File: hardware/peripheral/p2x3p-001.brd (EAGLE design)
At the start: 18 x 31 mm, 4 parts, among them J4 RLY

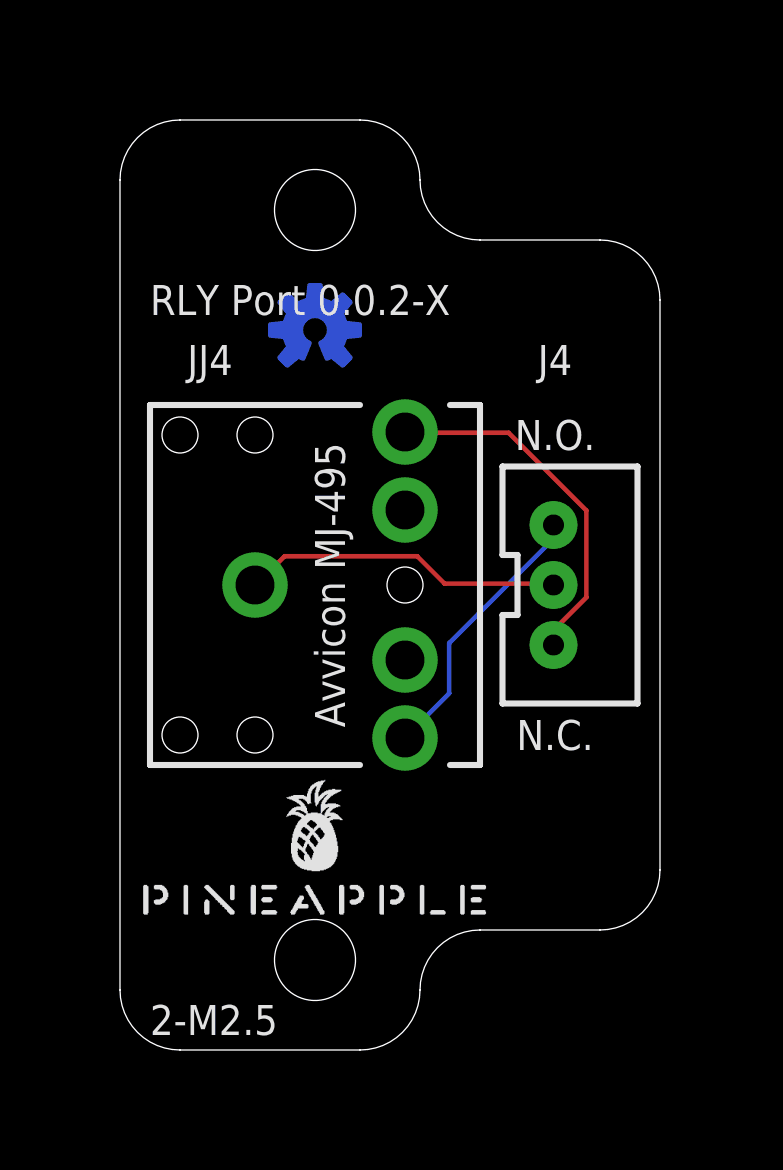
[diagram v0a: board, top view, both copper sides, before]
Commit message: Imported (again) from Hex Sw 0.0.2-X.
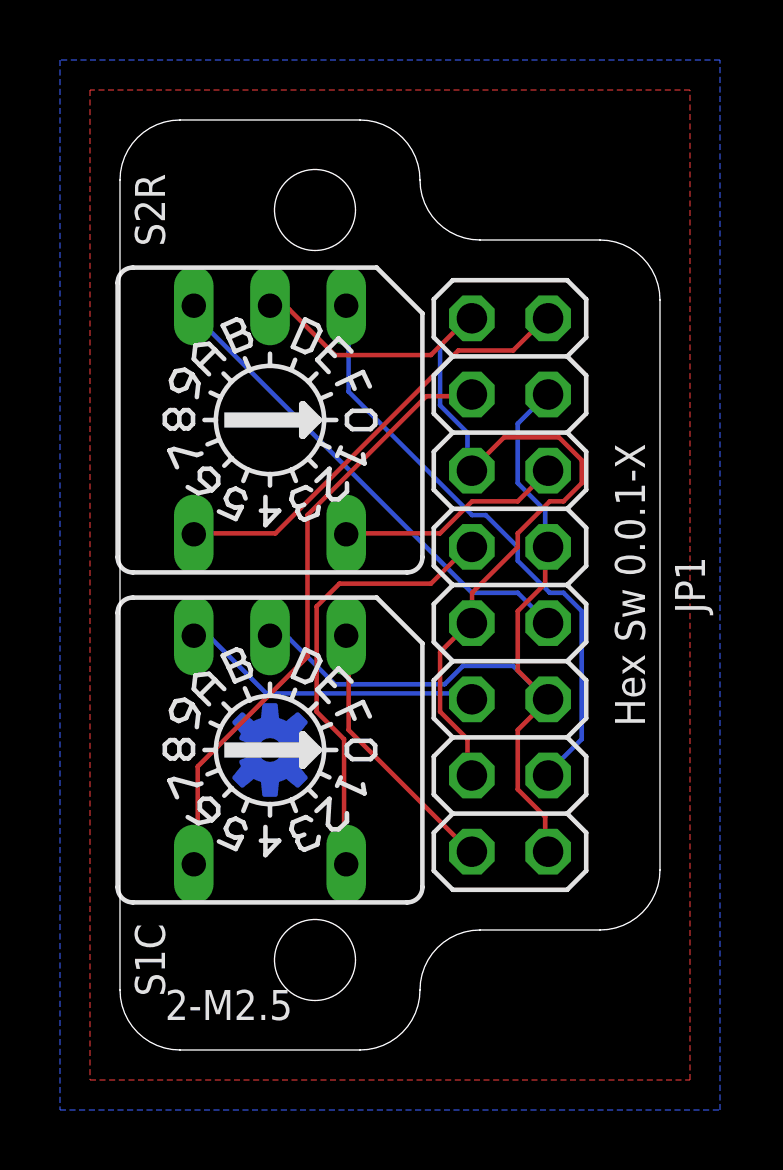
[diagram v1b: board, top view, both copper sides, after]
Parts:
- removed J4: RLY, SparkFun-Connectors:JST-3-PTH-VERT
- removed JJ4: AUDIO_JACK_3.5MM_KIT, SparkFun-Connectors:AUDIO-JACK-KIT
- added JP1: (no value), pinhead:2X08
- added S1C, S2R: (no value), switch-dil:A1353HEX
- moved U$1 17.6 mm to (0.50, 21.0), flipped to the bottom, turned to 90 degrees
- moved LOGO1 14.1 mm to (5.00, 10.0), turned to 90 degrees
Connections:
- removed net COMMON: J4.2, JJ4.SLEEVE
- removed net NC: J4.3, JJ4.RING
- removed net NO: J4.1, JJ4.TIP
- new net ANLG0: JP1.3, S2R.1
- new net ANLG1: JP1.7, S2R.4
- new net ANLG2: JP1.11, S2R.8
- new net ANLG3: JP1.15, S2R.2
- new net DTCT0: JP1.2, S1C.1
- new net DTCT1: JP1.6, S1C.4
- new net DTCT2: JP1.10, S1C.8
- new net DTCT3: JP1.14, S1C.2
- new net GND: JP1.1, JP1.13, JP1.5, JP1.9, S1C.C
- new net VCC: JP1.12, JP1.16, JP1.4, JP1.8, S2R.C
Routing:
- net VCC: track 0.00 -> 31.7 mm
- net GND: track 0.00 -> 28.5 mm
- net DTCT3: track 0.00 -> 20.4 mm
- net ANLG0: track 0.00 -> 19.9 mm
- net ANLG1: track 0.00 -> 16.4 mm
- net DTCT2: track 0.00 -> 15.0 mm
- net ANLG3: track 0.00 -> 14.8 mm
- net NC: track 12.1 -> 0.00 mm
- net COMMON: track 10.7 -> 0.00 mm
- net DTCT1: track 0.00 -> 10.1 mm
- net NO: track 9.15 -> 0.00 mm
- net DTCT0: track 0.00 -> 8.95 mm
- net ANLG2: track 0.00 -> 7.60 mm
- added copper zone on layer 1, net GND
- added copper zone on layer 16, net GND
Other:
- board text added: "A0"
- board text added: "A1"
- board text added: "A2"
- board text added: "A3"
- board text added: "D10"
- board text added: "D12"
- board text added: "D6"
- board text added: "D9"
- board text added: "G"
- board text added: "Hex Sw 0.0.1-X"
- board text added: "V/2"
- board text removed: "Avvicon MJ-495"
- board text removed: "N.C."
- board text removed: "N.O."
- board text removed: "RLY Port 0.0.2-X"
- board text removed: "Ring"
- board text removed: "Sleeve"
- board text removed: "T-R-S=NO-NC-Common"
- board text removed: "Tip"

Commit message: WIP.
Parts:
- removed S1C, S2R: (no value), switch-dil:A1353HEX
- added J1, J2: (no value), SparkFun-Connectors:JST-3-PTH
- moved LOGO1 5.85 mm to (3.00, 15.5)
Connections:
- net ANLG0: no longer S2R.1
- net ANLG1: no longer S2R.4
- net ANLG2: no longer S2R.8
- net ANLG3: no longer S2R.2
- net DTCT0: no longer S1C.1
- net DTCT1: no longer S1C.4
- net DTCT2: no longer S1C.8
- net DTCT3: no longer S1C.2
- net GND: no longer S1C.C
- net VCC: no longer S2R.C
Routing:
- net VCC: track 31.7 -> 0.00 mm
- net GND: track 28.5 -> 0.00 mm
- net DTCT3: track 20.4 -> 0.00 mm
- net ANLG0: track 19.9 -> 0.00 mm
- net ANLG1: track 16.4 -> 0.00 mm
- net DTCT2: track 15.0 -> 0.00 mm
- net ANLG3: track 14.8 -> 0.00 mm
- net DTCT1: track 10.1 -> 0.00 mm
- net DTCT0: track 8.95 -> 0.00 mm
- net ANLG2: track 7.60 -> 0.00 mm
- removed copper zone on layer 1, net GND
- removed copper zone on layer 16, net GND
